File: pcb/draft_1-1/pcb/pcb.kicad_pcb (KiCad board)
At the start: 2 copper layers, 5 parts, among them J1 USB4110-GF-A, U1 H3LIS200DLTR, U2 ATSAML21G16B-AUT

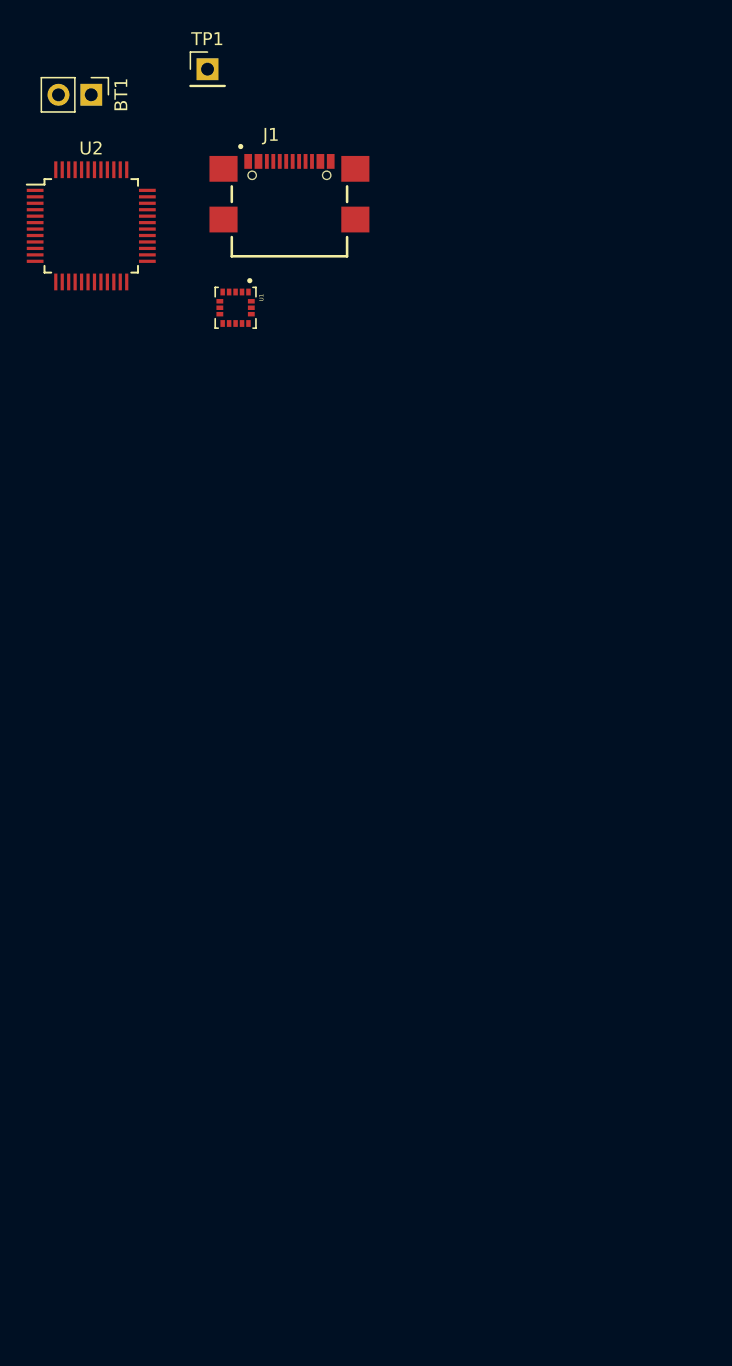
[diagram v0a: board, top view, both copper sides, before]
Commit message: PRE-TRACE PLACEMENT CHECKPOINT
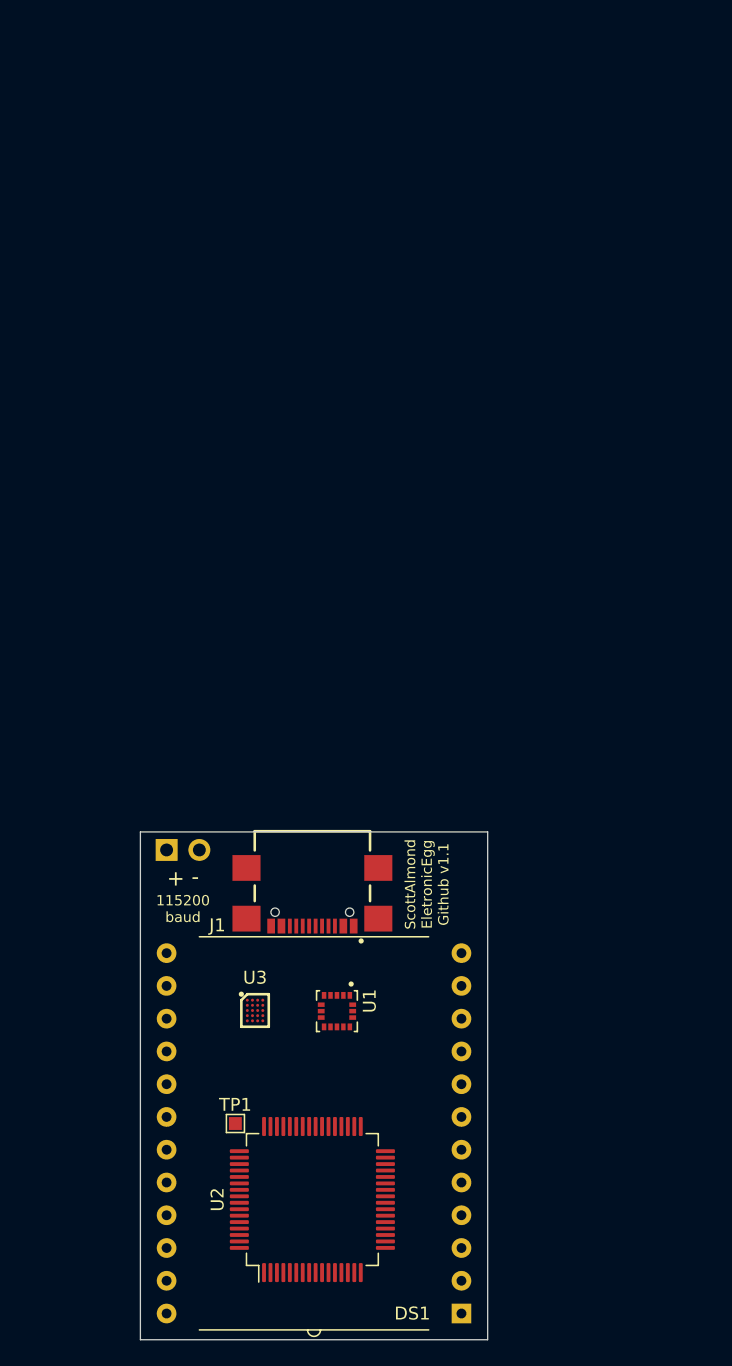
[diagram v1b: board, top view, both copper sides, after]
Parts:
- added DS1: VI-321-DP-RC-S, custom:VI-321-DP-RC-S, F.Cu at (140.5, 111.0)
- added U3: BQ25155, SamacSys_Parts:BGA20C40P4X5_162X202X50, F.Cu at (135.9, 101.5)
- BT1: moved to B.Cu
- TP1: footprint Connector_PinHeader_2.54mm:PinHeader_1x01_P2.54mm_Vertical -> TestPoint:TestPoint_Pad_1.0x1.0mm
- U2: value ATSAML21G16B-AUT -> ATSAML21J16B-AUT; footprint Package_QFP:TQFP-48_7x7mm_P0.5mm -> Package_QFP:TQFP-64_10x10mm_P0.5mm
- moved TP1 81.8 mm to (134.4, 110.2)
- moved U2 77.4 mm to (140.3, 116.1), turned to 90 degrees
- moved BT1 58.8 mm to (129.0, 89.0)
- moved J1 57.2 mm to (140.3, 93.9), turned to 180 degrees
- moved U1 55.1 mm to (142.2, 101.5)
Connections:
- U2 pad 17: Net-(U2-Pad17) -> /3E
- U2 pad 18: GND -> Net-(U2-Pad18)
- U2 pad 21: Net-(U2-Pad21) -> +3V3
- U2 pad 22: Net-(U2-Pad22) -> GND
- U2 pad 23: Net-(U2-Pad23) -> /1A
- U2 pad 28: INT3 -> Net-(U2-Pad28)
- U2 pad 29: INT2 -> Net-(U2-Pad29)
- U2 pad 30: INT1 -> Net-(U2-Pad30)
- U2 pad 31: SDA -> Net-(U2-Pad31)
- U2 pad 32: SCL -> Net-(U2-Pad32)
- U2 pad 33: D- -> GND
- U2 pad 34: D+ -> +3V3
- U2 pad 35: GND -> Net-(U2-Pad35)
- U2 pad 36: Net-(U2-Pad17) -> Net-(U2-Pad36)
- U2 pad 42: GND -> Net-(U2-Pad42)
- U2 pad 45: Net-(U2-Pad45) -> D-
- U2 pad 46: Net-(U2-Pad46) -> D+
- U2 pad 47: Net-(U2-Pad47) -> GND
- U2 pad 48: Net-(U2-Pad48) -> +3V3
- U2 pad 5: GND -> Net-(U2-Pad5)
- U2 pad 7: Net-(U2-Pad7) -> GND
- U2 pad 8: Net-(U2-Pad8) -> +1V8
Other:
- board outline added: 26.9 x 39.4 mm
- net class Default: clearance 0.2 -> 0.15; trace_width 0.25 -> 0.1524; via_dia 0.8 -> 0.508; via_drill 0.4 -> 0.254
- rule solder_mask_min_width: 0.25 -> 0.1016
- rule trace_clearance: 0.2 -> 0.15
- rule trace_min: 0.2 -> 0.15
- rule via_min_drill: 0.3 -> 0.254
- rule via_min_size: 0.4 -> 0.508
- board text added: "+ -"
- board text added: "- +"
- board text added: "115200 baud"
- board text added: "ScottAlmond EletronicEgg Github v1.1"

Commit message: attempt to route display
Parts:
- removed TP1: TestPoint, TestPoint:TestPoint_Pad_1.0x1.0mm
- added C1: 1uF, Capacitor_SMD:C_0402_1005Metric, F.Cu at (158.0, 98.4)
- added C2: 2.2uF, Capacitor_SMD:C_0402_1005Metric, F.Cu at (158.0, 100.4)
- added C3: 22uF, Capacitor_SMD:C_0402_1005Metric, F.Cu at (160.9, 98.4)
- added C4: 2.2uF, Capacitor_SMD:C_0402_1005Metric, F.Cu at (158.0, 102.4)
- added C5: 2.2uF, Capacitor_SMD:C_0402_1005Metric, F.Cu at (160.9, 100.4)
- added C6: 100nF, Capacitor_SMD:C_0402_1005Metric, F.Cu at (163.8, 98.4)
- added C7: 100nF, Capacitor_SMD:C_0402_1005Metric, F.Cu at (158.0, 104.4)
- added C8: 100nF, Capacitor_SMD:C_0402_1005Metric, F.Cu at (160.9, 102.4)
- added C9: 1uF, Capacitor_SMD:C_0402_1005Metric, F.Cu at (163.8, 100.4)
- added L1: 10uH, Inductor_SMD:L_0805_2012Metric, F.Cu at (146.3, 107.7)
- added R1: 10k, Resistor_SMD:R_0402_1005Metric, F.Cu at (160.9, 104.4)
- added R2: 10k, Resistor_SMD:R_0402_1005Metric, F.Cu at (163.8, 102.4)
- added R3: 10k, Resistor_SMD:R_0402_1005Metric, F.Cu at (166.7, 100.4)
- added R4: 56k, Resistor_SMD:R_0402_1005Metric, F.Cu at (128.9, 93.3)
- added R5: 10k, Resistor_SMD:R_0402_1005Metric, F.Cu at (163.8, 104.4)
- added R6: 56k, Resistor_SMD:R_0402_1005Metric, F.Cu at (131.3, 93.3)
- added R7: 10k, Resistor_SMD:R_0402_1005Metric, F.Cu at (169.6, 100.4)
- added TH1: Thermistor_NTC, Resistor_SMD:R_0402_1005Metric, F.Cu at (166.7, 104.4)
- turned U2 to 315 degrees
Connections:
- net Net-(C1-Pad1) renamed +5V
- DS1 pad 1: /3E -> /13
- DS1 pad 10: /1D -> /22
- DS1 pad 11: /1C -> /23
- DS1 pad 12: /1B -> /24
- DS1 pad 13: /1A -> /1
- DS1 pad 14: /1F -> /2
- DS1 pad 15: /1G -> /3
- DS1 pad 16: /2B -> /4
- DS1 pad 17: /2A -> /5
- DS1 pad 18: /2F -> /6
- DS1 pad 19: /2G -> /7
- DS1 pad 2: /3D -> /14
- DS1 pad 20: /3B -> /8
- DS1 pad 21: /3A -> /9
- DS1 pad 22: /3F -> /10
- DS1 pad 23: /3G -> /11
- DS1 pad 24: /COM -> /12
- DS1 pad 3: /3C -> /15
- DS1 pad 4: /3DP -> /16
- DS1 pad 5: /2E -> /17
- DS1 pad 6: /2D -> /18
- DS1 pad 7: /2C -> /19
- DS1 pad 8: /2DP -> /20
- DS1 pad 9: /1E -> /21
- U1 pad 14: +3V3 -> +1V8
- U1 pad 15: +3V3 -> +1V8
- U2 pad 14: Net-(U2-Pad14) -> INT3
- U2 pad 15: Net-(U2-Pad15) -> INT2
- U2 pad 16: Net-(U2-Pad16) -> INT1
- U2 pad 17: /3E -> /1
- U2 pad 18: Net-(U2-Pad18) -> /2
- U2 pad 19: Net-(U2-Pad19) -> /3
- U2 pad 20: Net-(U2-Pad20) -> /4
- U2 pad 21: +3V3 -> +1V8
- U2 pad 23: /1A -> /5
- U2 pad 24: Net-(U2-Pad24) -> /6
- U2 pad 25: Net-(U2-Pad25) -> /7
- U2 pad 26: Net-(U2-Pad26) -> /8
- U2 pad 27: Net-(U2-Pad27) -> /9
- U2 pad 28: Net-(U2-Pad28) -> /10
- U2 pad 29: Net-(U2-Pad29) -> /11
- U2 pad 30: Net-(U2-Pad30) -> /12
- U2 pad 31: Net-(U2-Pad31) -> /13
- U2 pad 32: Net-(U2-Pad32) -> /14
- U2 pad 34: +3V3 -> +1V8
- U2 pad 35: Net-(U2-Pad35) -> /15
- U2 pad 36: Net-(U2-Pad36) -> /16
- U2 pad 37: Net-(U2-Pad37) -> /17
- U2 pad 38: Net-(U2-Pad38) -> /18
- U2 pad 39: Net-(U2-Pad39) -> /19
- U2 pad 40: Net-(U2-Pad40) -> /20
- U2 pad 41: Net-(U2-Pad41) -> /21
- U2 pad 42: Net-(U2-Pad42) -> /22
- U2 pad 43: Net-(U2-Pad43) -> /23
- U2 pad 44: Net-(U2-Pad44) -> /24
- U2 pad 48: +3V3 -> +1V8
- U2 pad 51: INT3 -> Net-(U2-Pad51)
- U2 pad 57: INT2 -> Net-(U2-Pad57)
- U2 pad 58: INT1 -> Net-(U2-Pad58)
- U3 pad D4: +3V3 -> +1V8
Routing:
- net GND: track 0.00 -> 26.6 mm
- net /1: track 0.00 -> 22.4 mm
- net /2: track 0.00 -> 21.5 mm
- net /3: track 0.00 -> 19.7 mm
- net /4: track 0.00 -> 17.9 mm
- net /5: track 0.00 -> 17.2 mm
- net /6: track 0.00 -> 15.4 mm
- net /7: track 0.00 -> 13.6 mm
- net /8: track 0.00 -> 11.8 mm
- net /12: track 0.00 -> 10.4 mm
- net /9: track 0.00 -> 10.1 mm
- net /10: track 0.00 -> 9.54 mm
- net /11: track 0.00 -> 9.18 mm
- net D+: track 0.00 -> 2.52 mm
- net D-: track 0.00 -> 2.46 mm
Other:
- board text added: "ScottAlmond EletronicEgg Github v1.1 115200 baud"
- board text removed: "115200 baud"
- board text removed: "ScottAlmond EletronicEgg Github v1.1"

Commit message: bom cost estimate
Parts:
- moved C8 26.5 mm to (144.4, 123.1)
- moved C6 21.0 mm to (144.7, 107.1), turned to 90 degrees
- moved C9 19.2 mm to (145.8, 107.1), turned to 90 degrees
- moved C1 14.9 mm to (143.2, 96.4)
- moved C7 11.4 mm to (146.9, 107.0), turned to 90 degrees
- moved L1 1.78 mm to (146.2, 109.5)
- turned U1 to 90 degrees
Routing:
- net /24: track 0.00 -> 25.7 mm
- net /23: track 0.00 -> 23.9 mm
- net /22: track 0.00 -> 22.1 mm
- net /21: track 0.00 -> 20.3 mm
- net /20: track 0.00 -> 18.5 mm
- net /19: track 0.00 -> 16.7 mm
- net /13: track 0.00 -> 15.5 mm
- net /18: track 0.00 -> 14.9 mm
- net /14: track 0.00 -> 13.7 mm
- net /17: track 0.00 -> 13.1 mm
- net /16: track 0.00 -> 11.4 mm
- net /15: track 0.00 -> 10.8 mm

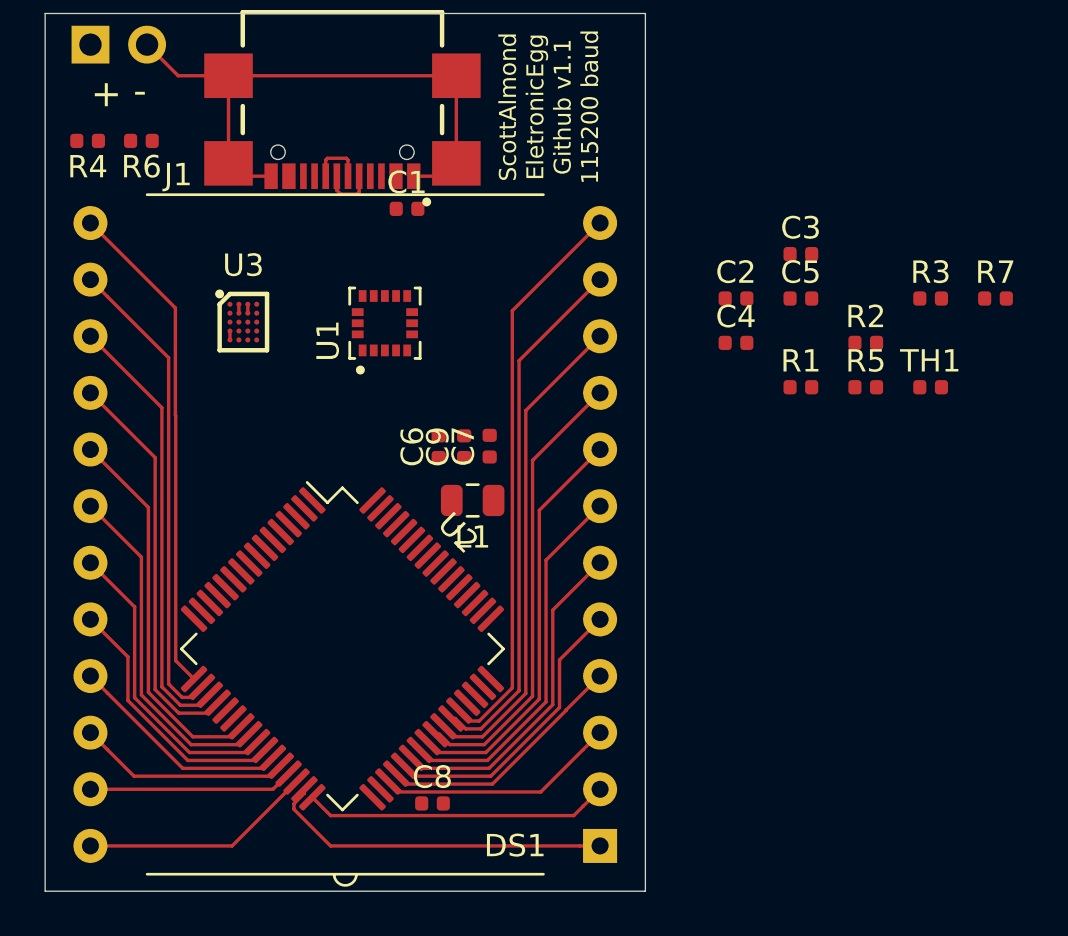
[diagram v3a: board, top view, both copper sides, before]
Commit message: maximized squid traces
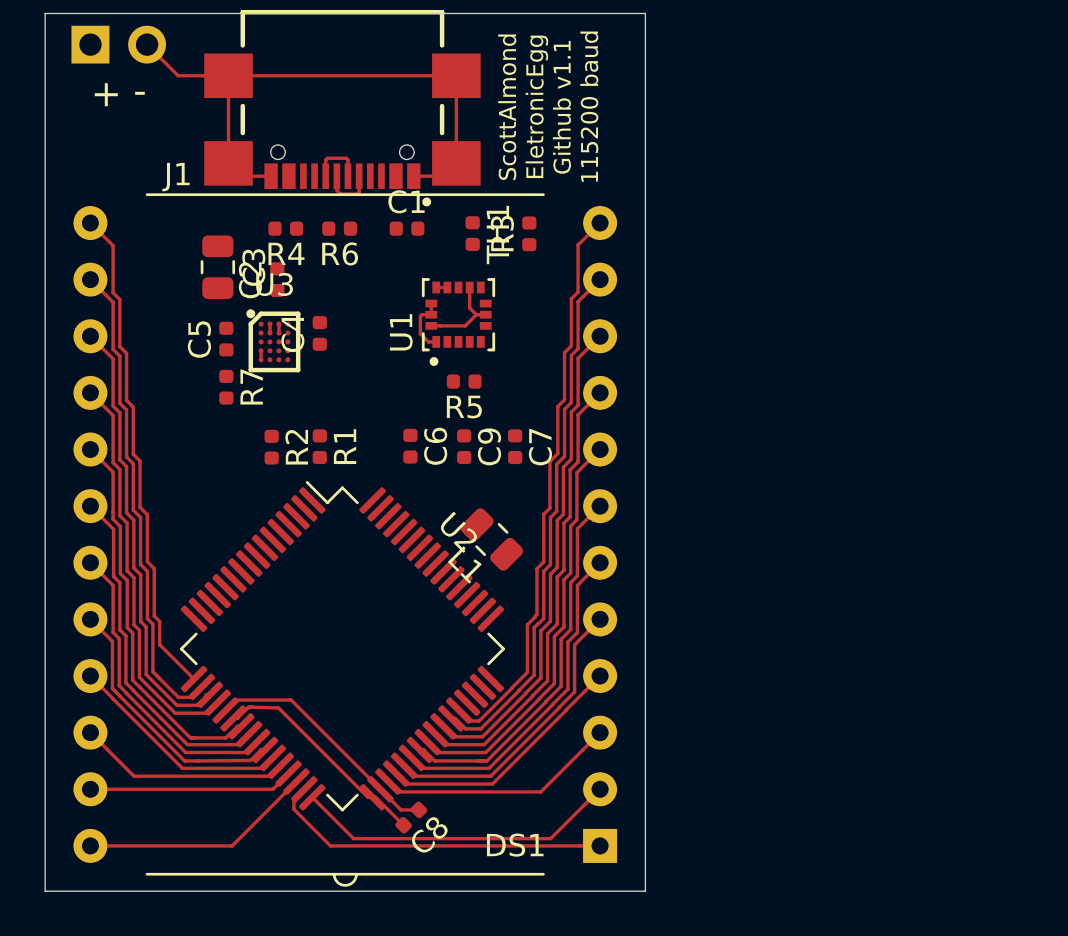
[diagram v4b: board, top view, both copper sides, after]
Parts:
- C3: footprint Capacitor_SMD:C_0402_1005Metric -> Capacitor_SMD:C_0805_2012Metric
- moved R7 34.7 mm to (135.1, 104.4), turned to 270 degrees
- moved R2 27.1 mm to (137.2, 107.1), turned to 270 degrees
- moved C3 26.2 mm to (134.7, 99.0), turned to 270 degrees
- moved C5 25.8 mm to (135.1, 102.2), turned to 90 degrees
- moved R1 21.7 mm to (139.3, 107.1), turned to 270 degrees
- moved TH1 21.7 mm to (146.2, 97.5), turned to 270 degrees
- moved C2 20.6 mm to (137.4, 99.6), turned to 90 degrees
- moved C4 18.7 mm to (139.3, 102.0), turned to 90 degrees
- moved R3 18.2 mm to (148.7, 97.5), turned to 90 degrees
- moved R5 18.0 mm to (145.8, 104.1), turned to 180 degrees
- moved R4 9.72 mm to (137.8, 97.3)
- moved R6 9.72 mm to (140.2, 97.3)
- moved U1 3.32 mm to (145.5, 101.1)
- moved L1 1.95 mm to (147.0, 111.2), turned to 135 degrees
- moved U3 1.66 mm to (137.3, 102.4)
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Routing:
- net GND: track 26.6 -> 41.3 mm
- net +1V8: track 0.40 -> 14.0 mm
- net /14: track 13.7 -> 14.6 mm

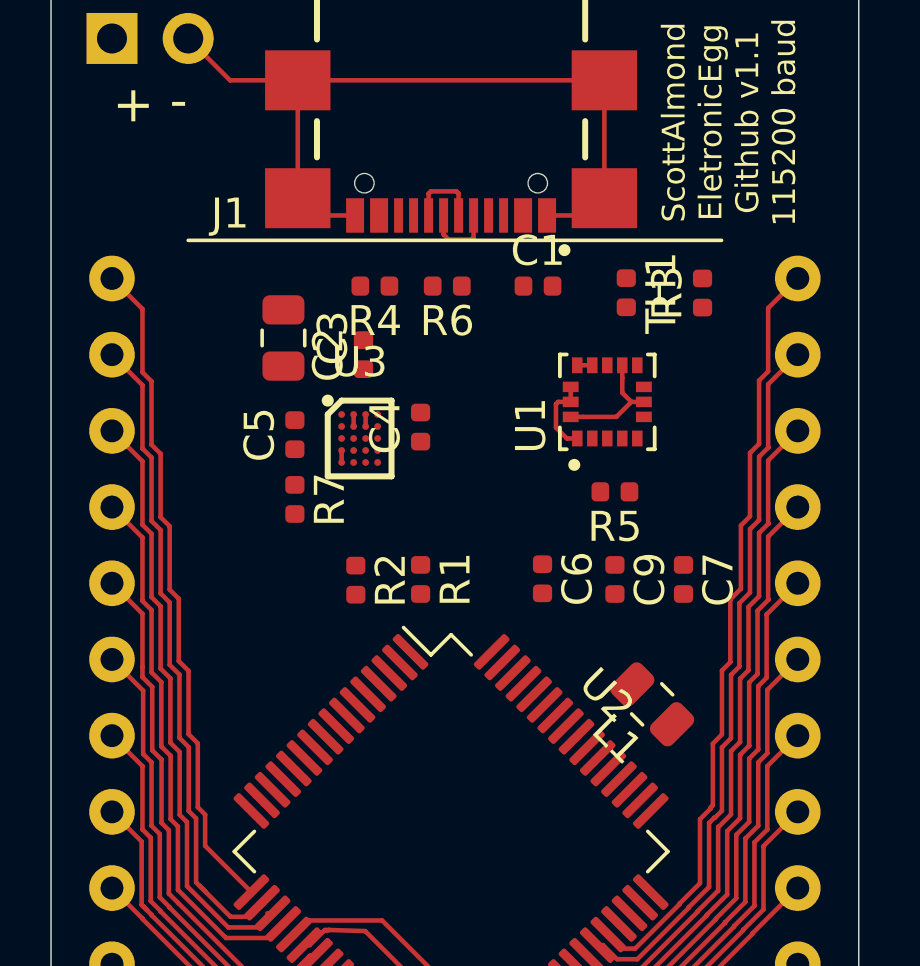
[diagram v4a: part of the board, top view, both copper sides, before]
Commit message: added accel decouple caps
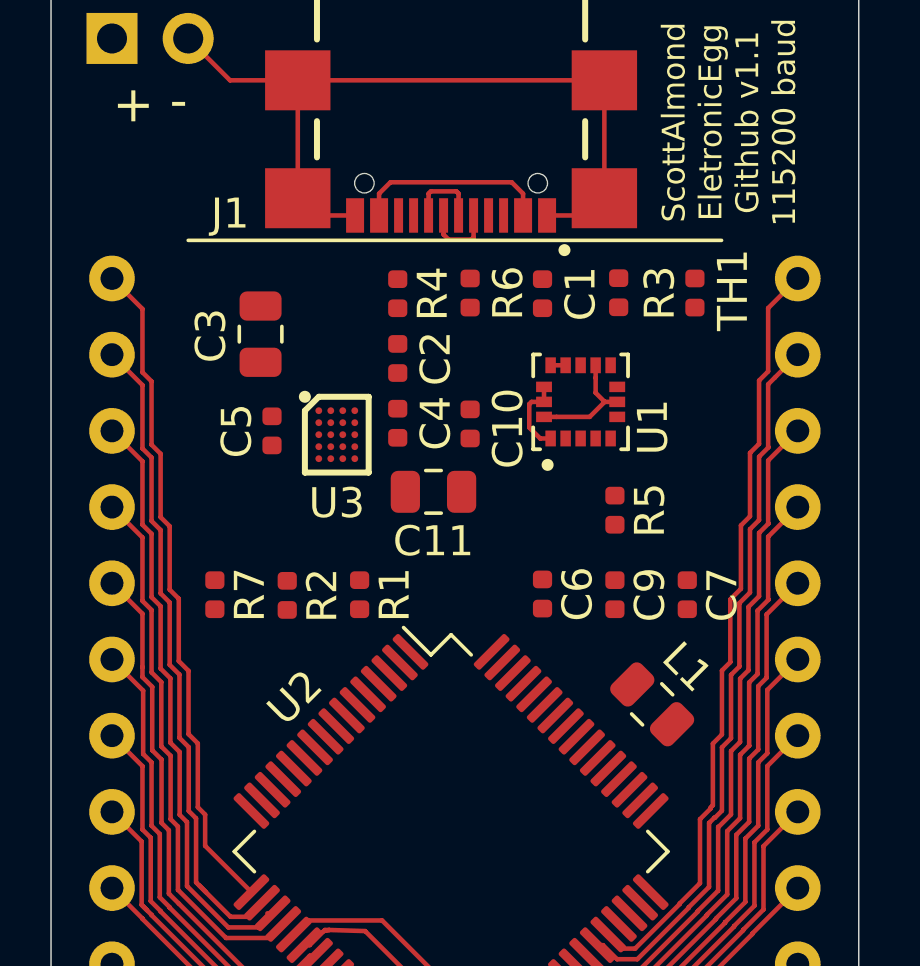
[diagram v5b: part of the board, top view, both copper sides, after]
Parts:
- added C10: 100nF, Capacitor_SMD:C_0402_1005Metric, F.Cu at (141.0, 101.9)
- added C11: 10uF, Capacitor_SMD:C_0805_2012Metric, F.Cu at (139.7, 104.1)
- moved R7 4.15 mm to (132.5, 107.6)
- moved R2 2.34 mm to (134.9, 107.6)
- moved R1 2.09 mm to (137.3, 107.6)
- moved C2 1.15 mm to (138.6, 99.7)
- moved U1 0.89 mm to (144.7, 101.1)
- moved R4 0.80 mm to (138.6, 97.5), turned to 270 degrees
- moved R6 0.80 mm to (141.0, 97.5), turned to 270 degrees
- moved C3 0.77 mm to (134.0, 98.9)
- moved C4 0.77 mm to (138.6, 101.9)
- moved U3 0.77 mm to (136.5, 102.2)
- moved C5 0.77 mm to (134.4, 102.1)
- moved R5 0.61 mm to (145.8, 104.8), turned to 270 degrees
- moved C7 0.52 mm to (148.2, 107.6)
- moved C6 0.51 mm to (143.4, 107.5)
- moved C9 0.51 mm to (145.8, 107.6)
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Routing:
- net +5V: track 0.00 -> 6.57 mm

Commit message: candidate layout done
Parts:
- moved C7 2.41 mm to (145.8, 107.6)
- moved C9 2.41 mm to (148.2, 107.5)
- moved R4 2.41 mm to (141.0, 97.5), turned to 90 degrees
- moved R6 2.41 mm to (138.6, 97.5), turned to 90 degrees
- moved C10 0.10 mm to (141.0, 102.0), turned to 270 degrees
- turned C2 to 270 degrees
- turned C1 to 270 degrees
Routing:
- net GND: track 41.3 -> 143.5 mm, vias 0 -> 6
- net +1V8: track 13.6 -> 92.2 mm, vias 0 -> 2
- net D+: track 2.52 -> 33.6 mm, vias 0 -> 2
- net SDA: track 0.00 -> 30.9 mm, vias 0 -> 3
- net D-: track 2.46 -> 32.1 mm, vias 0 -> 2
- net INT1: track 0.00 -> 28.9 mm, vias 0 -> 2
- net SCL: track 0.00 -> 28.1 mm, vias 0 -> 3
- net INT2: track 0.00 -> 25.0 mm, vias 0 -> 2
- net Net-(BT1-Pad1): track 0.00 -> 20.6 mm
- net INT3: track 0.00 -> 17.3 mm
- net Net-(R3-Pad1): track 0.00 -> 13.7 mm, vias 0 -> 2
- net Net-(C3-Pad2): track 0.00 -> 12.0 mm, vias 0 -> 2
- net Net-(C7-Pad1): track 0.00 -> 10.8 mm
- net +5V: track 6.57 -> 16.5 mm, vias 0 -> 2
- net Net-(R5-Pad1): track 0.00 -> 7.15 mm
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
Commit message: as built
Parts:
- C11: value 10uF -> 22uF
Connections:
- net /1 renamed /1A
- net /10 renamed /3F
- net /11 renamed /3G
- net /12 renamed /COM
- net /13 renamed /3E
- net /14 renamed /3D
- net /15 renamed /3C
- net /16 renamed /3DP
- net /17 renamed /2E
- net /18 renamed /2D
- net /19 renamed /2C
- net /2 renamed /1F
- net /20 renamed /2DP
- net /21 renamed /1E
- net /22 renamed /1D
- net /23 renamed /1C
- net /24 renamed /1B
- net /3 renamed /1G
- net /4 renamed /2B
- net /5 renamed /2A
- net /6 renamed /2F
- net /7 renamed /2G
- net /8 renamed /3B
- net /9 renamed /3A
